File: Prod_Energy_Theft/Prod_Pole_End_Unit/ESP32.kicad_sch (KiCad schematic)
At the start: 24 parts, among them J14 U.FL-R-SMT_01_, U13 USBLC6-2SC6, U14 E32-433T20S, U15 CP2102N-Axx-xQFN20, U16 ESP32-C6-MINI-1

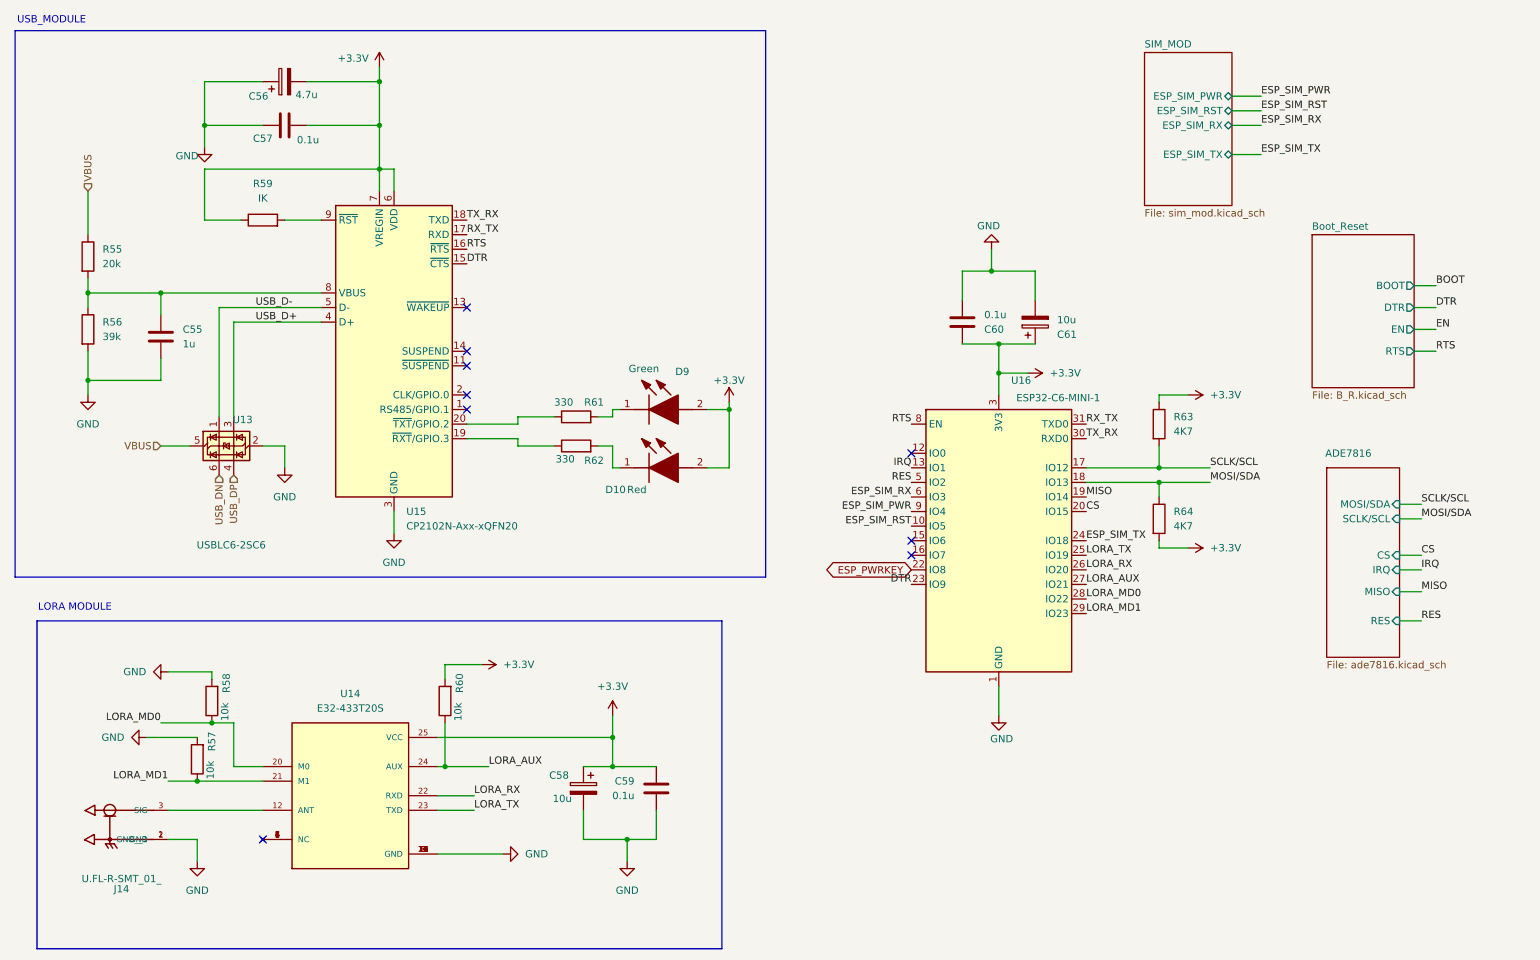
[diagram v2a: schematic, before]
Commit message: update in BOM list
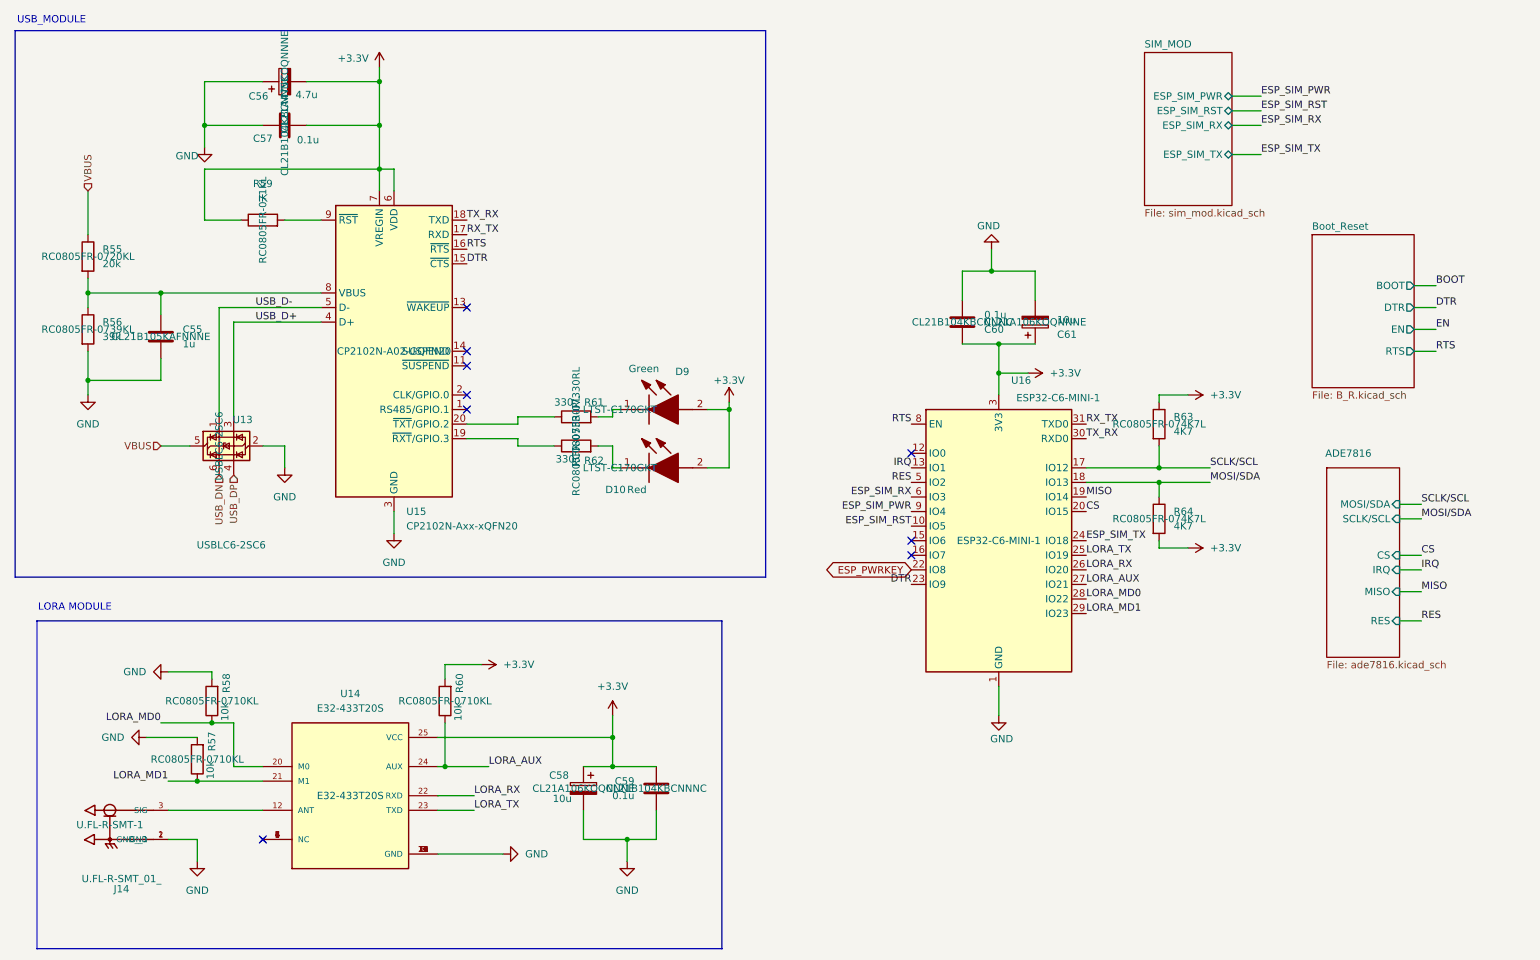
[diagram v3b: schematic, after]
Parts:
- C55: Part Number (none) -> CL21B105KAFNNNE
- C56: Part Number (none) -> CL21A475KOQNNNE
- C57, C59, C60: Part Number (none) -> CL21B104KBCNNNC
- C58, C61: Part Number (none) -> CL21A106KOQNNNE
- D10, D9: Part Number (none) -> LTST-C170GKT
- J14: Part Number (none) -> U.FL-R-SMT-1
- R55: Part Number (none) -> RC0805FR-0720KL
- R56: Part Number (none) -> RC0805FR-0739KL
- R57, R58, R60: Part Number (none) -> RC0805FR-0710KL
- R59: Part Number (none) -> RC0805FR-071KL
- R61, R62: Part Number (none) -> RC0805FR-07330RL
- R63, R64: Part Number (none) -> RC0805FR-074K7L
- U13: Part Number (none) -> USBLC6-2SC6
- U14: Part Number (none) -> E32-433T20S
- U15: Part Number (none) -> CP2102N-A02-GQFN20
- U16: Part Number (none) -> ESP32-C6-MINI-1
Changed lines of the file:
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@@
 			)
 		)
+		(property "Part Number" "RC0805FR-0739KL "
+			(at 30.48 69.85 0)
+			(effects
+				(font
+					(size 1.27 1.27)
+				)
+			)
+		)
 		(pin "2"
 		)
@@
 			)
 		)
+		(property "Part Number" "CL21A106KOQNNNE "
+			(at 116.84 149.86 0)
+			(effects
+				(font
+					(size 1.27 1.27)
+				)
+			)
+		)
 		(pin "1"
 		)
@@
 			)
 		)
+		(property "Part Number" "RC0805FR-07330RL "
+			(at 115.57 85.09 0)
+			(effects
+				(font
+					(size 1.27 1.27)
+				)
+			)
+		)
 		(pin "2"
 		)
@@
 			)
 		)
+		(property "Part Number" "U.FL-R-SMT-1 "
+			(at 34.29 156.21 0)
+			(effects
+				(font
+					(size 1.27 1.27)
+				)
+			)
+		)
 		(pin "2"
 		)
@@
 			)
 		)
+		(property "Part Number" "RC0805FR-0720KL "
+			(at 30.48 57.15 0)
+			(effects
+				(font
+					(size 1.27 1.27)
+				)
+			)
+		)
 		(pin "2"
 		)
@@
 			)
 		)
+		(property "Part Number" "E32-433T20S "
+			(at 76.2 151.13 0)
+			(effects
+				(font
+					(size 1.27 1.27)
+				)
+			)
+		)
 		(pin "4"
 		)
@@
 			)
 		)
+		(property "Part Number" "LTST-C170GKT "
+			(at 123.19 83.82 0)
+			(effects
+				(font
+					(size 1.27 1.27)
+				)
+			)
+		)
 		(pin "2"
 		)
@@
 			)
 		)
+		(property "Part Number" "CL21B104KBCNNNC "
+			(at 64.77 34.29 0)
+			(effects
+				(font
+					(size 1.27 1.27)
+				)
+			)
+		)
 		(pin "1"
 		)
@@
 			)
 		)
+		(property "Part Number" "CL21B104KBCNNNC "
+			(at 129.54 149.86 0)
+			(effects
+				(font
+					(size 1.27 1.27)
+				)
+			)
+		)
 		(pin "1"
 		)
@@
 			)
 		)
+		(property "Part Number" "CL21A475KOQNNNE "
+			(at 64.77 26.67 0)
+			(effects
+				(font
+					(size 1.27 1.27)
+				)
+			)
+		)
 		(pin "1"
 		)
@@
 			)
 		)
+		(property "Part Number" "ESP32-C6-MINI-1 "
+			(at 189.23 106.68 0)
+			(effects
+				(font
+					(size 1.27 1.27)
+				)
+			)
+		)
 		(pin "2"
 		)
@@
 			)
 		)
+		(property "Part Number" "RC0805FR-0710KL "
+			(at 92.71 134.62 0)
+			(effects
+				(font
+					(size 1.27 1.27)
+				)
+			)
+		)
 		(pin "2"
 		)
@@
 			)
 		)
+		(property "Part Number" "RC0805FR-071KL "
+			(at 60.96 50.8 0)
+			(effects
+				(font
+					(size 1.27 1.27)
+				)
+			)
+		)
 		(pin "1"
 		)
@@
 			)
 		)
+		(property "Part Number" "RC0805FR-074K7L "
+			(at 217.17 86.36 0)
+			(effects
+				(font
+					(size 1.27 1.27)
+				)
+			)
+		)
 		(pin "1"
 		)
@@
 			)
 		)
+		(property "Part Number" "CL21B105KAFNNNE "
+			(at 43.18 71.12 0)
+			(effects
+				(font
+					(size 1.27 1.27)
+				)
+			)
+		)
 		(pin "2"
 		)
@@
 			)
 		)
+		(property "Part Number" "RC0805FR-0710KL "
+			(at 52.07 134.62 0)
+			(effects
+				(font
+					(size 1.27 1.27)
+				)
+			)
+		)
 		(pin "2"
 		)
@@
 			)
 		)
+		(property "Part Number" "CP2102N-A02-GQFN20 "
+			(at 83.82 73.66 0)
+			(effects
+				(font
+					(size 1.27 1.27)
+				)
+			)
+		)
 		(pin "3"
 		)
@@
 			)
 		)
+		(property "Part Number" "LTST-C170GKT "
+			(at 123.19 93.98 0)
+			(effects
+				(font
+					(size 1.27 1.27)
+				)
+			)
+		)
 		(pin "2"
 		)
@@
 			)
 		)
+		(property "Part Number" "CL21A106KOQNNNE "
+			(at 195.58 68.58 0)
+			(effects
+				(font
+					(size 1.27 1.27)
+				)
+			)
+		)
 		(pin "1"
 		)
@@
 			)
 		)
+		(property "Part Number" "USBLC6-2SC6 "
+			(at 53.34 90.17 0)
+			(effects
+				(font
+					(size 1.27 1.27)
+				)
+			)
+		)
 		(pin "4"
 		)
@@
 			)
 		)
+		(property "Part Number" "RC0805FR-074K7L "
+			(at 217.17 102.87 0)
+			(effects
+				(font
+					(size 1.27 1.27)
+				)
+			)
+		)
 		(pin "1"
 		)
@@
 			)
 		)
+		(property "Part Number" "CL21B104KBCNNNC "
+			(at 182.88 68.58 0)
+			(effects
+				(font
+					(size 1.27 1.27)
+				)
+			)
+		)
 		(pin "1"
 		)
@@
 			)
 		)
+		(property "Part Number" "RC0805FR-07330RL "
+			(at 115.57 90.17 0)
+			(effects
+				(font
+					(size 1.27 1.27)
+				)
+			)
+		)
 		(pin "2"
 		)
@@
 			)
 		)
+		(property "Part Number" "RC0805FR-0710KL "
+			(at 49.53 144.78 0)
+			(effects
+				(font
+					(size 1.27 1.27)
+				)
+			)
+		)
